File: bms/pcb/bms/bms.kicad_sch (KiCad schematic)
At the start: 17 parts, among them U8 Pico

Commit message: v1.0 of BMS finalised. Sent of for fabrication
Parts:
- removed BATT-1-CAN1, BATT-2-CAN1, MAIN-CAN1: MCP2515-xSO, Package_SO:SOIC-18W_7.5x11.6mm_P1.27mm, symbol Interface_CAN_LIN:MCP2515-xSO
- removed PS1: TPS62160DGKT, Module:SOP65P490X110-8N, symbol MCU_Module:TPS62160DGKT
- added C5, C6: 1uF, Capacitor_SMD:C_0603_1608Metric, symbol Device:C_Polarized_Small_US
- added H1, H2, H3, H4: MountingHole, MountingHole:MountingHole_3.2mm_M3, symbol Mechanical:MountingHole
- added IC1, IC2: NCV8402ASTT1G, SOT230P700X175-4N, symbol Transistor_FET:NCV8402ASTT1G
- added IC3, IC4, IC5: MCP2515-I_ST, SOP65P640X120-20N, symbol MCU_Module:MCP2515-I_ST
- added IC9: TPS62160DGKR, SOP65P490X110-8N, symbol power:TPS62160DGKR
- added J1: power, 105430YY02, symbol Connector:1054301102
- added J2: MAIN CAN, 105430YY02, symbol Connector:1054301102
- added J3: BATT1 CAN, 105430YY02, symbol Connector:1054301102
- added J4: BATT2 CAN, 105430YY02, symbol Connector:1054301102
- added J5, J6: INPUTS, 105430YY02, symbol Connector:1054301102
- added R10, R8, R9: 120, Resistor_SMD:R_0805_2012Metric, symbol Device:R_US
- added R4, R5: 4k7, Resistor_SMD:R_0805_2012Metric, symbol Device:R_Small_US
- added R6, R7: 1k5, Resistor_SMD:R_0805_2012Metric, symbol Device:R_Small_US
- R1, R2, R3: footprint Resistor_SMD:R_0201_0603Metric -> Resistor_SMD:R_0805_2012Metric
- renumbered BATT-2-TXVR1 to IC6, BATT-1-TXVR1 to IC7, MAIN-CAN-TXVR1 to IC8
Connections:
- net 12V: now also IC9.2 (VIN), IC9.3 (EN), J1.1
- net 3V: now also IC3.20 (VDD), IC4.20 (VDD), IC5.20 (VDD)
- net 5V: now also IC9.6 (VOS)
- net 8MHz: now also U8.31 (GPIO26_ADC0), IC3.9 (OSC1), IC4.9 (OSC1), IC5.9 (OSC1); no longer U8.9 (GPIO6)
- net BATT_1_CAN_H: now also J3.1, R9.2
- net BATT_1_CAN_L: now also J3.2, R9.1
- net BATT_1_CAN_RX: now also IC4.2 (RXCAN)
- net BATT_1_CAN_TX: now also IC4.1 (TXCAN)
- net BATT_1_CS: now also U8.29 (GPIO22), IC4.18 (~{CS}); no longer U8.20 (GPIO15)
- net BATT_2_CAN_H: now also J4.1, R10.2
- net BATT_2_CAN_L: now also J4.2, R10.1
- net BATT_2_CAN_RX: now also IC5.2 (RXCAN)
- net BATT_2_CAN_TX: now also IC5.1 (TXCAN)
- net BATT_2_CS: now also U8.20 (GPIO15), IC5.18 (~{CS})
- net GND: now also U8.13 (GND), U8.18 (GND), U8.38 (GND), U8.8 (GND), C5.2, C6.2, IC1.3 (S), IC2.3 (S), IC3.10 (VSS), IC4.10 (VSS), IC5.10 (VSS), J1.2, R6.2, R7.2; no longer U8.42 (GND)
- net MAIN_CAN_CS: now also IC3.18 (~{CS})
- net MAIN_CAN_H: now also J2.1, R8.2
- net MAIN_CAN_L: now also J2.2, R8.1
- net MAIN_CAN_RX: now also IC3.2 (RXCAN)
- net MAIN_CAN_TX: now also IC3.1 (TXCAN)
- net SPI0_CLK: now also IC3.14 (SCK), IC4.14 (SCK), IC5.14 (SCK)
- net SPI0_MISO: now also IC3.17 (SO), IC4.17 (SO), IC5.17 (SO)
- net SPI0_MOSI: now also IC3.16 (SI), IC4.16 (SI), IC5.16 (SI)
- net at C1.2, C4.2, R3.2: now also IC9.1 (PGND), IC9.4 (AGND)
- net at R2.2, R3.1: now also IC9.5 (FB)
- net at L1.1: now also IC9.7 (SW)
- net UART_TX: now reaches U8.1 (GPIO0)
- net CHARGE_ENABLE_IN_SIGNAL: now reaches U8.14 (GPIO10)
- net CHARGE_ENABLE_IN_SIGNAL: now also C6.1, R5.2, R7.1
- net IGNITION_ON_IN_SIGNAL: now reaches U8.15 (GPIO11)
- net IGNITION_ON_IN_SIGNAL: now also C5.1, R4.2, R6.1
- net UART_RX: now reaches U8.2 (GPIO1)
- net BATT_1_CONTACTOR_SIGNAL: now reaches U8.4 (GPIO2)
- net BATT_1_CONTACTOR_SIGNAL: now also IC1.1 (G)
- net BATT_2_CONTACTOR_SIGNAL: now reaches U8.5 (GPIO3)
- net BATT_2_CONTACTOR_SIGNAL: now also IC2.1 (G)
- net at R1.2: now also IC9.8 (PG)
- net SPI0_CS: no longer names the net of U8.7 (GPIO5)
- new net BATT_1_CONTACTOR_GND: IC1.2 (D_1), J6.2
- new net BATT_2_CONTACTOR_GND: IC2.2 (D_1), J6.1
- new net CHARGE_ENABLE_IN: J5.2, R5.1
- new net IGNITION_ON_IN: J5.1, R4.1
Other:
- moved on the sheet: C1, C2, C3, C4, D1, IC6, IC7, IC8, L1, R1, R2, R3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

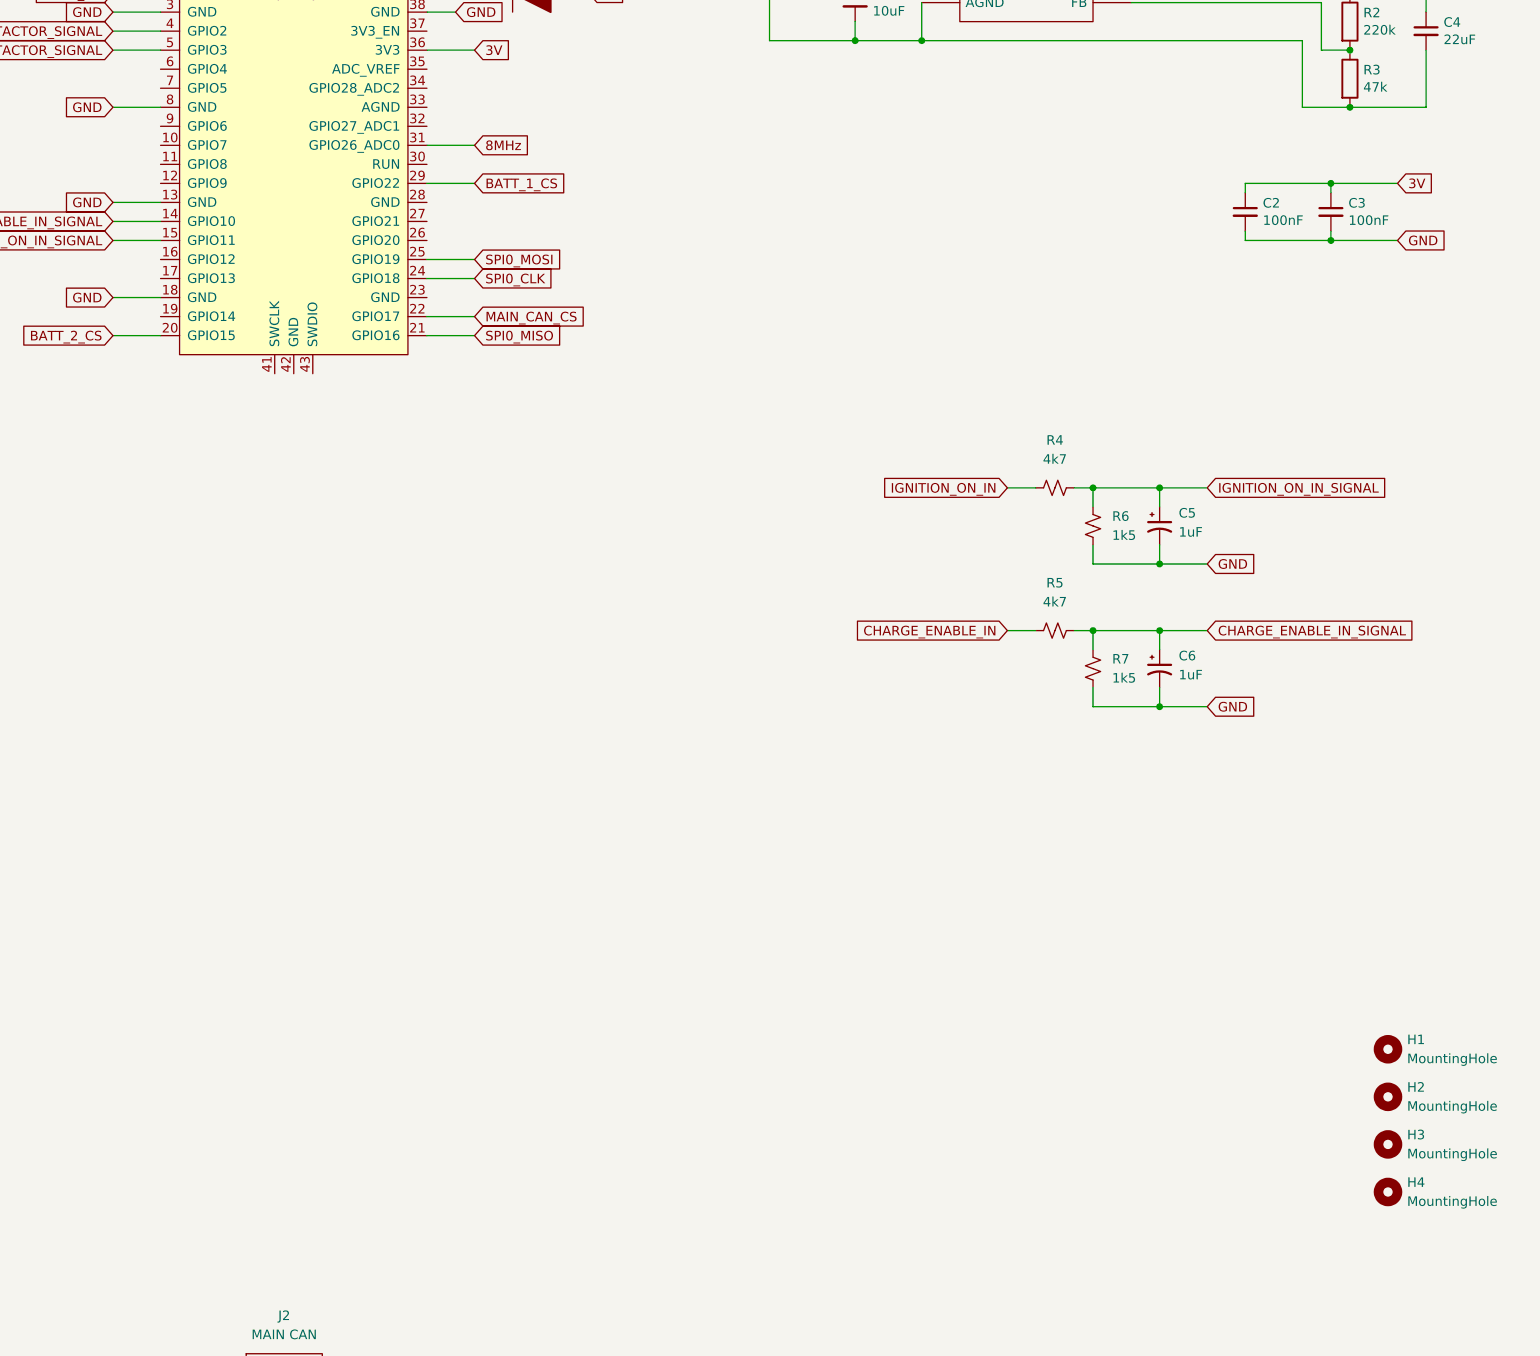
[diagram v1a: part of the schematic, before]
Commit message: BMS PCB fixes. Serial header for debugging. Heavier traces in certain places. Fix some pico pin connections.
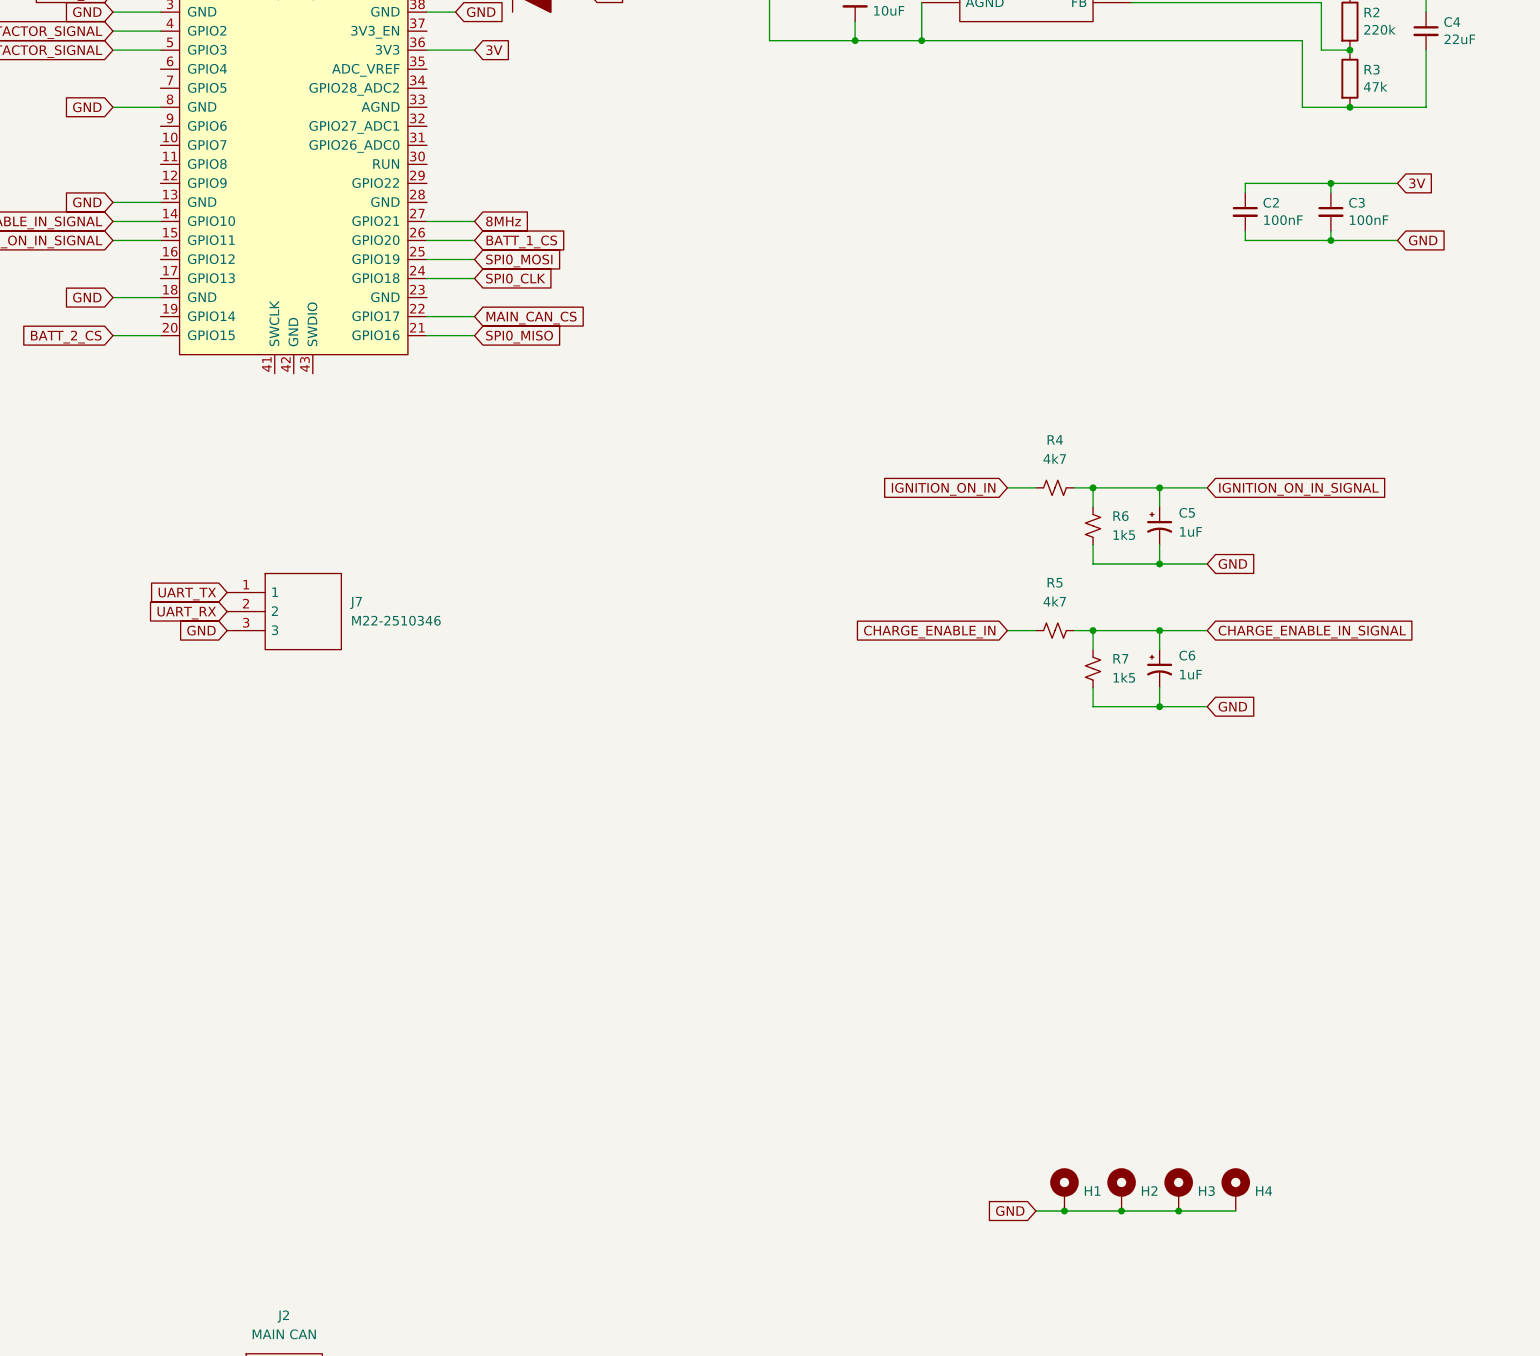
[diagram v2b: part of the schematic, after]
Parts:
- removed H1, H2, H3, H4: MountingHole, MountingHole:MountingHole_3.2mm_M3, symbol Mechanical:MountingHole
- added H1, H2, H3, H4: MountingHole, MountingHole:MountingHole_3.2mm_M3_Pad, symbol Mechanical:MountingHole_Pad
- added J7: M22-2510346, HDRV3W50P0X200_1X3_600X200X525P, symbol Connector:M22-2510346
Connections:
- net 8MHz: now also U8.27 (GPIO21); no longer U8.31 (GPIO26_ADC0)
- net BATT_1_CS: now also U8.26 (GPIO20); no longer U8.29 (GPIO22)
- net GND: now also H1.1, H2.1, H3.1, H4.1, J7.3
- net UART_RX: now also J7.2
- net UART_TX: now also J7.1

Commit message: Found two more errors in bms. Create version 3
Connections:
- net 3V: now also IC3.19 (~{RESET}), IC4.19 (~{RESET}), IC5.19 (~{RESET})
- net GND: now also C1.2, C4.2, IC9.1 (PGND), IC9.4 (AGND), R3.2
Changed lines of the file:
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@@
   (junction (at 391.16 30.48) (diameter 0) (color 0 0 0 0)
   )
+  (junction (at 391.16 49.53) (diameter 0) (color 0 0 0 0)
+  )
   (junction (at 381 41.91) (diameter 0) (color 0 0 0 0)
   )
@@
     (stroke (width 0) (type default) (color 0 0 0 0))
   )
+  (wire (pts (xy 80.01 57.15) (xy 80.01 59.69))
+    (stroke (width 0) (type default) (color 0 0 0 0))
+  )
   (wire (pts (xy 147.32 39.37) (xy 151.13 39.37))
     (stroke (width 0) (type default) (color 0 0 0 0))
@@
     (stroke (width 0) (type default) (color 0 0 0 0))
   )
+  (wire (pts (xy 391.16 49.53) (xy 397.51 49.53))
+    (stroke (width 0) (type default) (color 0 0 0 0))
+  )
   (wire (pts (xy 377.19 41.91) (xy 381 41.91))
     (stroke (width 0) (type default) (color 0 0 0 0))
@@
     (stroke (width 0) (type default) (color 0 0 0 0))
   )
+  (wire (pts (xy 80.01 218.44) (xy 80.01 220.98))
+    (stroke (width 0) (type default) (color 0 0 0 0))
+  )
   (wire (pts (xy 228.6 248.92) (xy 234.95 248.92))
     (stroke (width 0) (type default) (color 0 0 0 0))
@@
     (stroke (width 0) (type default) (color 0 0 0 0))
   )
+  (wire (pts (xy 80.01 138.43) (xy 80.01 140.97))
+    (stroke (width 0) (type default) (color 0 0 0 0))
+  )
   (wire (pts (xy 367.03 67.31) (xy 367.03 66.04))
     (stroke (width 0) (type default) (color 0 0 0 0))
@@
     )
   )
+  (global_label "GND" (shape input) (at 397.51 49.53 0) (fields_autoplaced)
+    (effects (font (size 1.27 1.27)) (justify left))
+    (property "Intersheet References" "${INTERSHEET_REFS}" (id 0) (at 57.15 -196.85 0)
+      (effects (font (size 1.27 1.27)) hide)
+    )
+  )

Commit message: BMS pcb v4
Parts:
- removed H1, H2, H3, H4: MountingHole, MountingHole:MountingHole_3.2mm_M3_Pad, symbol Mechanical:MountingHole_Pad
- removed J1: power, 105430YY02, symbol Connector:1054301102
- removed J2: MAIN CAN, 105430YY02, symbol Connector:1054301102
- removed J3: BATT1 CAN, 105430YY02, symbol Connector:1054301102
- removed J4: BATT2 CAN, 105430YY02, symbol Connector:1054301102
- removed J5, J6: INPUTS, 105430YY02, symbol Connector:1054301102
- added C10, C7, C8, C9: 1uF, Capacitor_SMD:C_0603_1608Metric, symbol Device:C_Polarized_Small_US
- added IC10, IC11, IC12, IC13: NCV8402ASTT1G, SOT230P700X175-4N, symbol Transistor_FET:NCV8402ASTT1G
- added JP1, JP2, JP3: SolderJumper_2_Open, Jumper:SolderJumper-2_P1.3mm_Open_Pad1.0x1.5mm, symbol Jumper:SolderJumper_2_Open
- added R11, R12, R13, R14: 4k7, Resistor_SMD:R_0805_2012Metric, symbol Device:R_Small_US
- added R15, R16, R17, R18: 1k5, Resistor_SMD:R_0805_2012Metric, symbol Device:R_Small_US
- added X1: ATM13-12PB-12PC-BM03, ATM1312PB12PCBM03, symbol Connector:ATM13-12PB-12PC-BM03
- J7: footprint HDRV3W50P0X200_1X3_600X200X525P -> Connector_PinHeader_2.54mm:PinHeader_1x03_P2.54mm_Vertical
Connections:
- net 12V: now also X1.B5
- net 5V: now also X1.B7, X1.B8
- net BATT_1_CAN_H: now also JP2.2 (B), X1.B2; no longer R9.2
- net BATT_1_CAN_L: now also X1.B11
- net BATT_2_CAN_H: now also JP3.2 (B), X1.B1; no longer R10.2
- net BATT_2_CAN_L: now also X1.B12
- net CHARGE_ENABLE_IN: now also X1.A3
- net CHARGE_ENABLE_IN_SIGNAL: now also U8.12 (GPIO9); no longer U8.14 (GPIO10)
- net GND: now also U8.23 (GND), U8.28 (GND), U8.33 (AGND), C10.2, C7.2, C8.2, C9.2, IC10.3 (S), IC11.3 (S), IC12.3 (S), IC13.3 (S), R15.2, R16.2, R17.2, R18.2, X1.B4, X1.B6, X1.B9
- net IGNITION_ON_IN: now also X1.A10
- net IGNITION_ON_IN_SIGNAL: now also U8.14 (GPIO10); no longer U8.15 (GPIO11)
- net MAIN_CAN_H: now also JP1.2 (B), X1.B3; no longer R8.2
- net MAIN_CAN_L: now also X1.B10
- net OUT_4_SIGNAL: now reaches U8.10 (GPIO7)
- net OUT_4_SIGNAL: now also IC13.1 (G)
- net IN_2_SIGNAL: now reaches U8.16 (GPIO12)
- net IN_2_SIGNAL: now also C8.1, R12.2, R16.1
- net IN_3_SIGNAL: now reaches U8.17 (GPIO13)
- net IN_3_SIGNAL: now also C9.1, R13.2, R17.1
- net IN_4_SIGNAL: now reaches U8.19 (GPIO14)
- net IN_4_SIGNAL: now also C10.1, R14.2, R18.1
- net OUT_1_SIGNAL: now reaches U8.6 (GPIO4)
- net OUT_1_SIGNAL: now also IC10.1 (G)
- net OUT_2_SIGNAL: now reaches U8.7 (GPIO5)
- net OUT_2_SIGNAL: now also IC11.1 (G)
- net OUT_3_SIGNAL: now reaches U8.9 (GPIO6)
- net OUT_3_SIGNAL: now also IC12.1 (G)
- net BATT_1_CONTACTOR_GND renamed BATT_1_INHIBIT
- net BATT_1_INHIBIT: now also X1.A7
- net BATT_1_CONTACTOR_SIGNAL renamed BATT_1_INHIBIT_SIGNAL
- net BATT_2_CONTACTOR_GND renamed BATT_2_INHIBIT
- net BATT_2_INHIBIT: now also X1.A6
- net BATT_2_CONTACTOR_SIGNAL renamed BATT_2_INHIBIT_SIGNAL
- new net: JP3.1 (A), R10.2
- new net: JP2.1 (A), R9.2
- new net: JP1.1 (A), R8.2
- new net IN_1: R11.1, X1.A2
- new net IN_1_SIGNAL: C7.1, R11.2, R15.1, U8.15 (GPIO11)
- new net IN_2: R12.1, X1.A11
- new net IN_3: R13.1, X1.A1
- new net IN_4: R14.1, X1.A12
- new net OUT_1: IC10.2 (D_1), X1.A5
- new net OUT_2: IC11.2 (D_1), X1.A8
- new net OUT_3: IC12.2 (D_1), X1.A4
- new net OUT_4: IC13.2 (D_1), X1.A9
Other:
- moved on the sheet: D1, R10, R8, R9
